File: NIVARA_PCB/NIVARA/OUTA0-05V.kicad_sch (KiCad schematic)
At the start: 0 parts

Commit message: SALIDAS DE VOLTAJE Y CORRIENTE
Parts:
- added C21: 1uF, PCM_Capacitor_SMD_AKL:C_0603_1608Metric, symbol PCM_Capacitor_AKL:C_0603
- added C22: 100nF, PCM_Capacitor_SMD_AKL:C_0603_1608Metric, symbol PCM_Capacitor_AKL:C_0603
- added D7: SM6T12A, Diode_SMD:D_SMB, symbol Diode:SM6T12A
- added R15: 0R, PCM_Resistor_SMD_AKL:R_0603_1608Metric, symbol PCM_Resistor_AKL:R_0603
- added U13: GP8201S-TC50-EW, easyeda2kicad:ESOP-8_L4.9-W3.9-P1.27-LS6.0-BL-EP, symbol easyeda2kicad:GP8201S-TC50-EW
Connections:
- net OUT_1: now also C22.2, D7.1 (A1), U13.6 (VOUT)
- new net: C21.2, R15.1, U13.8 (V5V)
- new net: R15.2, U13.7 (SEL)
- new net GND: C21.1, C22.1, D7.2 (A2), U13.5 (GND), U13.9 (EP)
- new net I2C.SDA: U13.2 (SDA)
- new net I2C.SLCK: U13.1 (SCLK)
- new net VCC: U13.4 (VCC)
- no-connect marks 0 -> 1

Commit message: ACTUALIZACION
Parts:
- C22: PART NUMBERT (none) -> CC0603KRX7R9BB104
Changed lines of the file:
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@@
 			)
 		)
-		(property "PART NUMBERT" ""
+		(property "PART NUMBERT" "CC0603KRX7R9BB104"
 			(at 93.98 60.96 0)
 			(effects

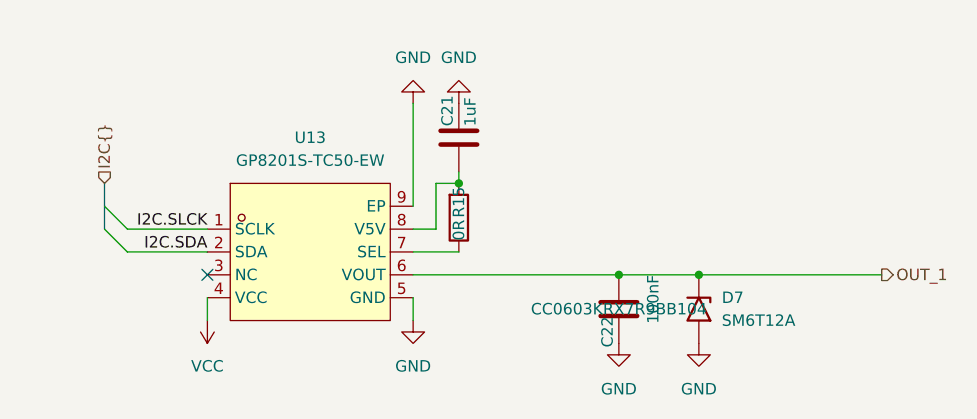
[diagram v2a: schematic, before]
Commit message: Se organizaron componentes en el area de PCB
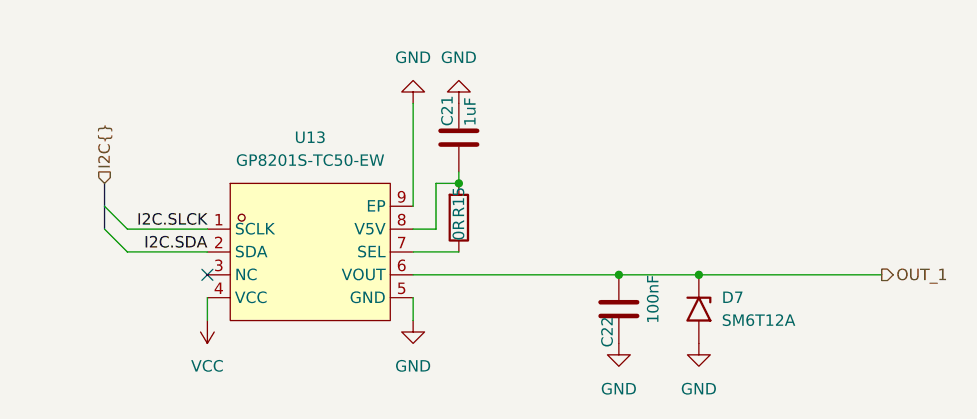
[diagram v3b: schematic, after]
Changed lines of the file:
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@@
 					(size 1.27 1.27)
 				)
+				(hide yes)
 			)
 		)

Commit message: arreglo del desastre que tenia con las salidas PNP
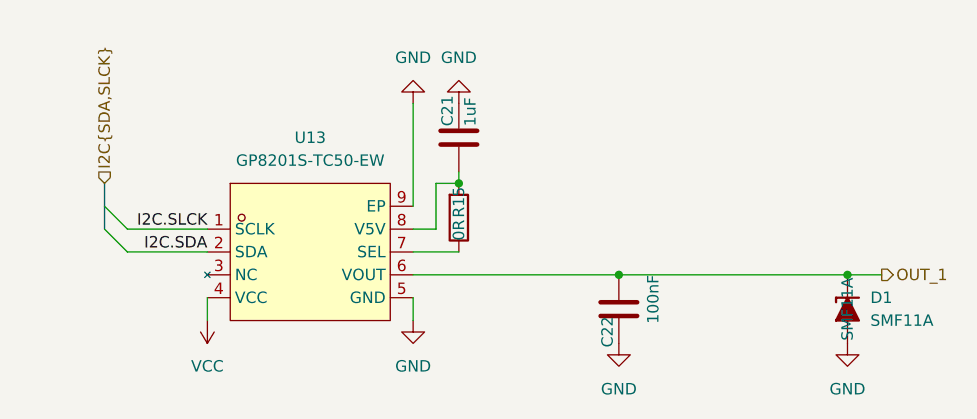
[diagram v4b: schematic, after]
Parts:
- removed D7: SM6T12A, Diode_SMD:D_SMB, symbol Diode:SM6T12A
- added D1: SMF11A, PCM_Diode_SMD_AKL:D_SOD-123F, symbol PCM_Diode_TVS_AKL:SMF11A
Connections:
- net GND: now also D1.2 (A)
- net OUT_1: now also D1.1 (K)
- no-connect marks 1 -> 0
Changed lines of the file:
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@@
 	(paper "A4")
 	(junction
-		(at 102.87 57.15)
+		(at 119.38 57.15)
 		(diameter 0)
 		(color 0 0 0 0)
@@
 		(color 0 0 0 0)
 	)
-	(no_connect
-		(at 48.26 57.15)
-	)
 	(bus_entry
 		(at 36.83 52.07)
@@
 	(wire
 		(pts
-			(xy 102.87 57.15) (xy 123.19 57.15)
+			(xy 119.38 57.15) (xy 123.19 57.15)
 		)
 		(stroke
@@
 	(wire
 		(pts
-			(xy 93.98 57.15) (xy 102.87 57.15)
+			(xy 93.98 57.15) (xy 119.38 57.15)
 		)
 		(stroke
@@
 		)
 	)
-	(hierarchical_label "I2C{}"
+	(hierarchical_label "I2C{SDA,SLCK}"
 		(shape input)
 		(at 36.83 46.99 90)
@@
 	(symbol
 		(lib_id "power:GND")
-		(at 102.87 64.77 0)
+		(at 119.38 64.77 0)
 		(unit 1)
 		(exclude_from_sim no)
@@
 		(dnp no)
 		(fields_autoplaced yes)
-		(property "Reference" "#PWR085"
-			(at 102.87 71.12 0)
+		(property "Reference" "#PWR096"
+			(at 119.38 71.12 0)
 			(effects
 				(font
@@
 		)
 		(property "Value" "GND"
-			(at 102.87 69.85 0)
+			(at 119.38 69.85 0)
 			(effects
 				(font
@@
 		)
 		(property "Footprint" ""
-			(at 102.87 64.77 0)
+			(at 119.38 64.77 0)
 			(effects
 				(font
@@
 		)
 		(property "Datasheet" ""
-			(at 102.87 64.77 0)
+			(at 119.38 64.77 0)
 			(effects
 				(font
@@
 		)
 		(property "Description" "Power symbol creates a global label with name \"GND\" , ground"
-			(at 102.87 64.77 0)
+			(at 119.38 64.77 0)
 			(effects
 				(font
@@
 			(project "NIVARA"
 				(path "/6298d7d5-28da-40bf-9586-24a8e5c02b82/7ff0dada-fc46-483c-91ad-b264be8c64cf/34eccd05-06f7-4b37-a228-f349577fb821"
-					(reference "#PWR085")
+					(reference "#PWR096")
 					(unit 1)
 				)
@@
 	)
 	(symbol
-		(lib_id "Diode:SM6T12A")
-		(at 102.87 60.96 270)
+		(lib_id "PCM_Diode_TVS_AKL:SMF11A")
+		(at 119.38 60.96 90)
 		(unit 1)
 		(exclude_from_sim no)
@@
 		(dnp no)
 		(fields_autoplaced yes)
-		(property "Reference" "D7"
-			(at 105.41 59.6899 90)
-			(effects
-				(font
-					(size 1.27 1.27)
-				)
-				(justify left)
-			)
-		)
-		(property "Value" "SM6T12A"
-			(at 105.41 62.2299 90)
-			(effects
-				(font
-					(size 1.27 1.27)
-				)
-				(justify left)
-			)
-		)
-		(property "Footprint" "Diode_SMD:D_SMB"
-			(at 97.79 60.96 0)
-			(effects
-				(font
-					(size 1.27 1.27)
-				)
-				(hide yes)
-			)
-		)
-		(property "Datasheet" "https://www.st.com/resource/en/datasheet/sm6t.pdf"
-			(at 102.87 59.69 0)
-			(effects
-				(font
-					(size 1.27 1.27)
-				)
-				(hide yes)
-			)
-		)
-		(property "Description" "600W unidirectional Transil Transient Voltage Suppressor, 12Vrwm, DO-214AA"
-			(at 102.87 60.96 0)
-			(effects
-				(font
-					(size 1.27 1.27)
-				)
-				(hide yes)
-			)
+		(property "Reference" "D1"
+			(at 121.92 59.6899 90)
+			(effects
+				(font
+					(size 1.27 1.27)
+				)
+				(justify right)
+			)
+		)
+		(property "Value" "SMF11A"
+			(at 121.92 62.2299 90)
+			(effects
+				(font
+					(size 1.27 1.27)
+				)
+				(justify right)
+			)
+		)
+		(property "Footprint" "PCM_Diode_SMD_AKL:D_SOD-123F"
+			(at 119.38 60.96 0)
+			(effects
+				(font
+					(size 1.27 1.27)
+				)
+				(hide yes)
+			)
+		)
+		(property "Datasheet" "https://www.tme.eu/Document/95faf1e5e821ed1b438500c66c7b0bd9/smf50a.pdf"
+			(at 119.38 60.96 0)
+			(effects
+				(font
+					(size 1.27 1.27)
+				)
+				(hide yes)
+			)
+		)
+		(property "Description" "SOD-123F Unidirectional TVS diode, 11V, 200W, Alternate KiCAD Library"
+			(at 119.38 60.96 0)
+			(effects
+				(font
+					(size 1.27 1.27)
+				)
+				(hide yes)
+			)
+		)
+		(property "PART NUMBERT" "SMF11A"
+			(at 119.38 60.96 0)
+			(effects
+				(font
+					(size 1.27 1.27)
+				)
+			)
+		)
+		(pin "1"
 		)
 		(pin "2"
 		)
-		(pin "1"
-		)
-		(instances
-			(project "NIVARA"
-				(path "/6298d7d5-28da-40bf-9586-24a8e5c02b82/7ff0dada-fc46-483c-91ad-b264be8c64cf/34eccd05-06f7-4b37-a228-f349577fb821"
-					(reference "D7")
-					(unit 1)
-				)
+		(instances
+			(project ""
+				(path "/6298d7d5-28da-40bf-9586-24a8e5c02b82/7ff0dada-fc46-483c-91ad-b264be8c64cf/34eccd05-06f7-4b37-a228-f349577fb821"
+					(reference "D1")
+					(unit 1)
+				)
